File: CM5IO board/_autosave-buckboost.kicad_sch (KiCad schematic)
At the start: 4 parts, among them IC1 TPS61089RNRR

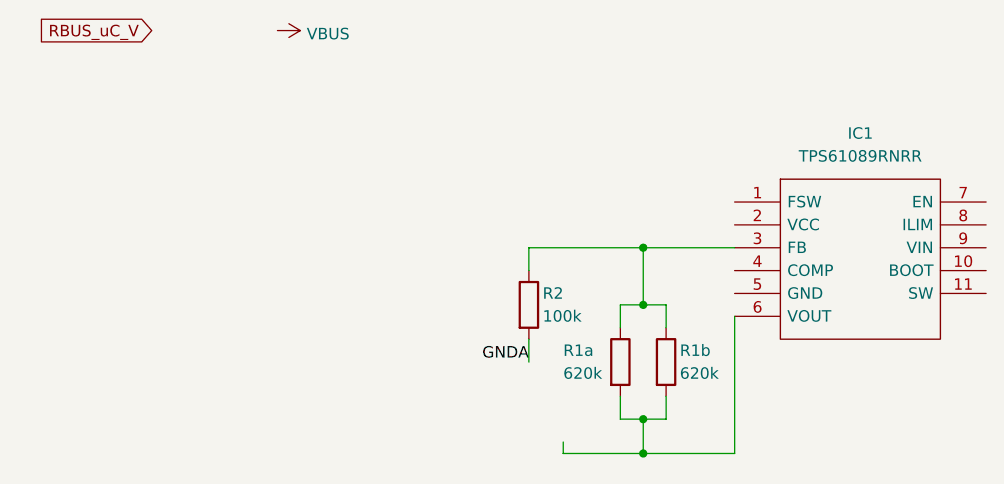
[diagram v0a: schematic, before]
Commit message: Began design of RBUS(4-5V)-to-CM5(5V) boost
R1, R2, R3 selected; Explained difference between GNDA and GND.
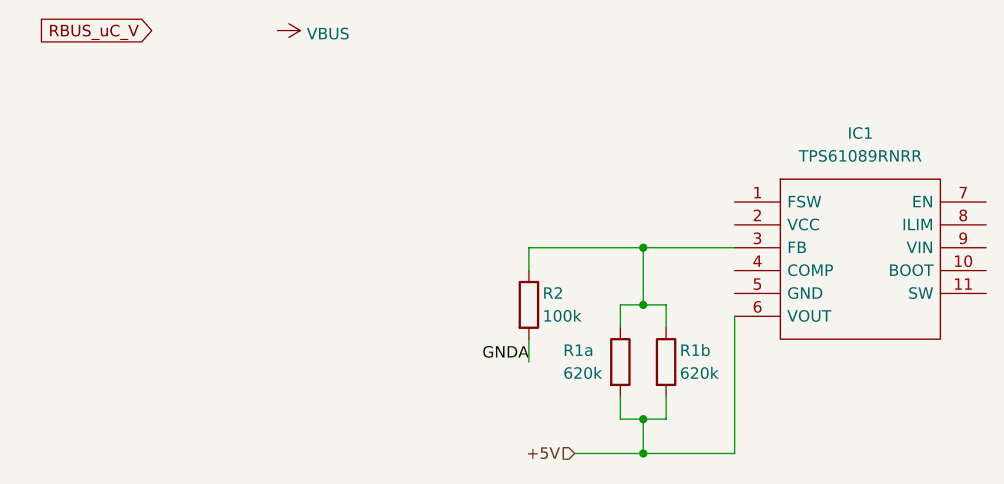
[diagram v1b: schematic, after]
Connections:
- net +5V: now reaches IC1.6 (VOUT), R1a.2, R1b.2
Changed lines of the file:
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@@
-	(wire
-		(pts
-			(xy 101.6 95.25) (xy 101.6 96.52)
-		)
-		(stroke
-			(width 0)
-			(type default)
-		)
-	)
 	(wire
 		(pts
@@
 	(wire
 		(pts
-			(xy 110.49 96.52) (xy 101.6 96.52)
+			(xy 110.49 96.52) (xy 102.87 96.52)
 		)
 		(stroke
@@
 		)
 	)
+	(hierarchical_label "+5V"
+		(shape input)
+		(at 102.87 96.52 180)
+		(effects
+			(font
+				(size 1.27 1.27)
+			)
+			(justify right)
+		)
+	)
